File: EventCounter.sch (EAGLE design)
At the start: 23 parts, among them J1 CONN_42.54_SCREW, Q1 2N7002, Q3 DMG3404, U7 MCP6041, U8 MCP6041

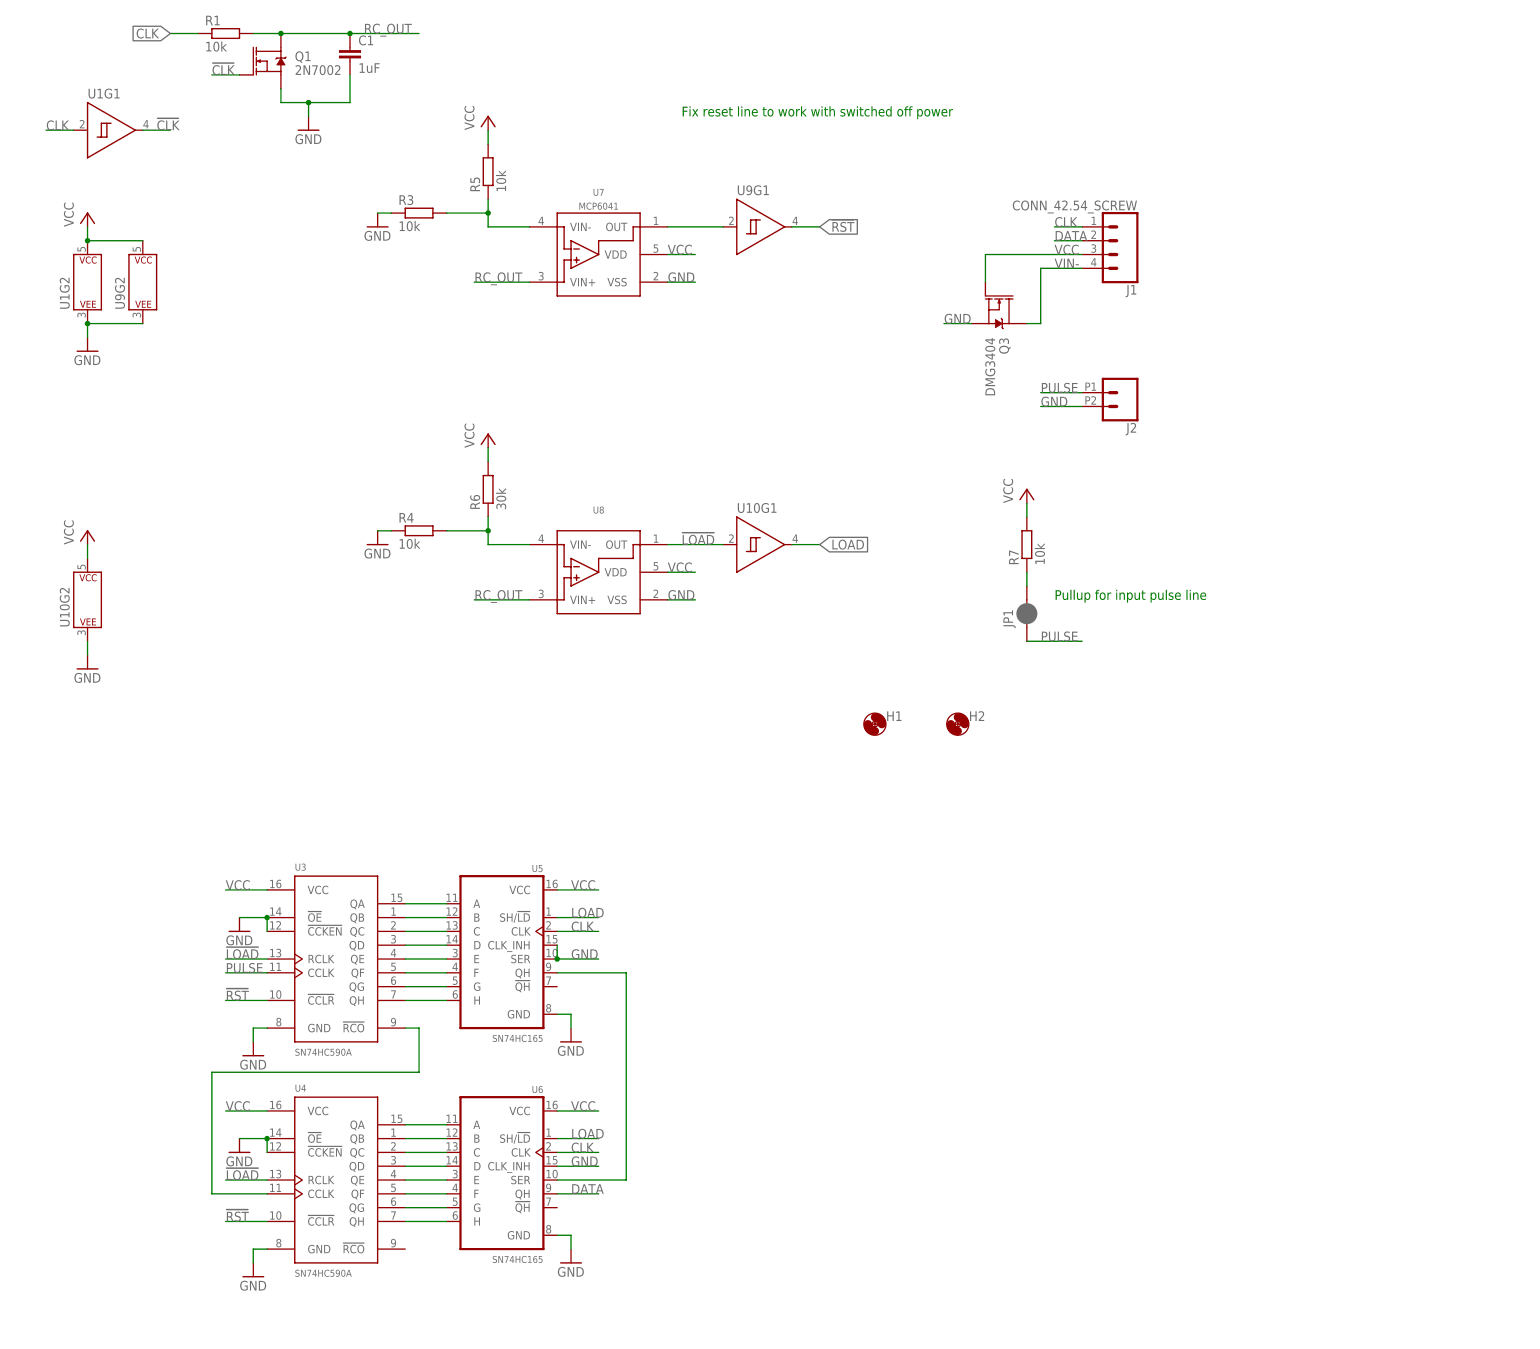
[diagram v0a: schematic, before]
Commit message: Cleaned up schematic and added frame
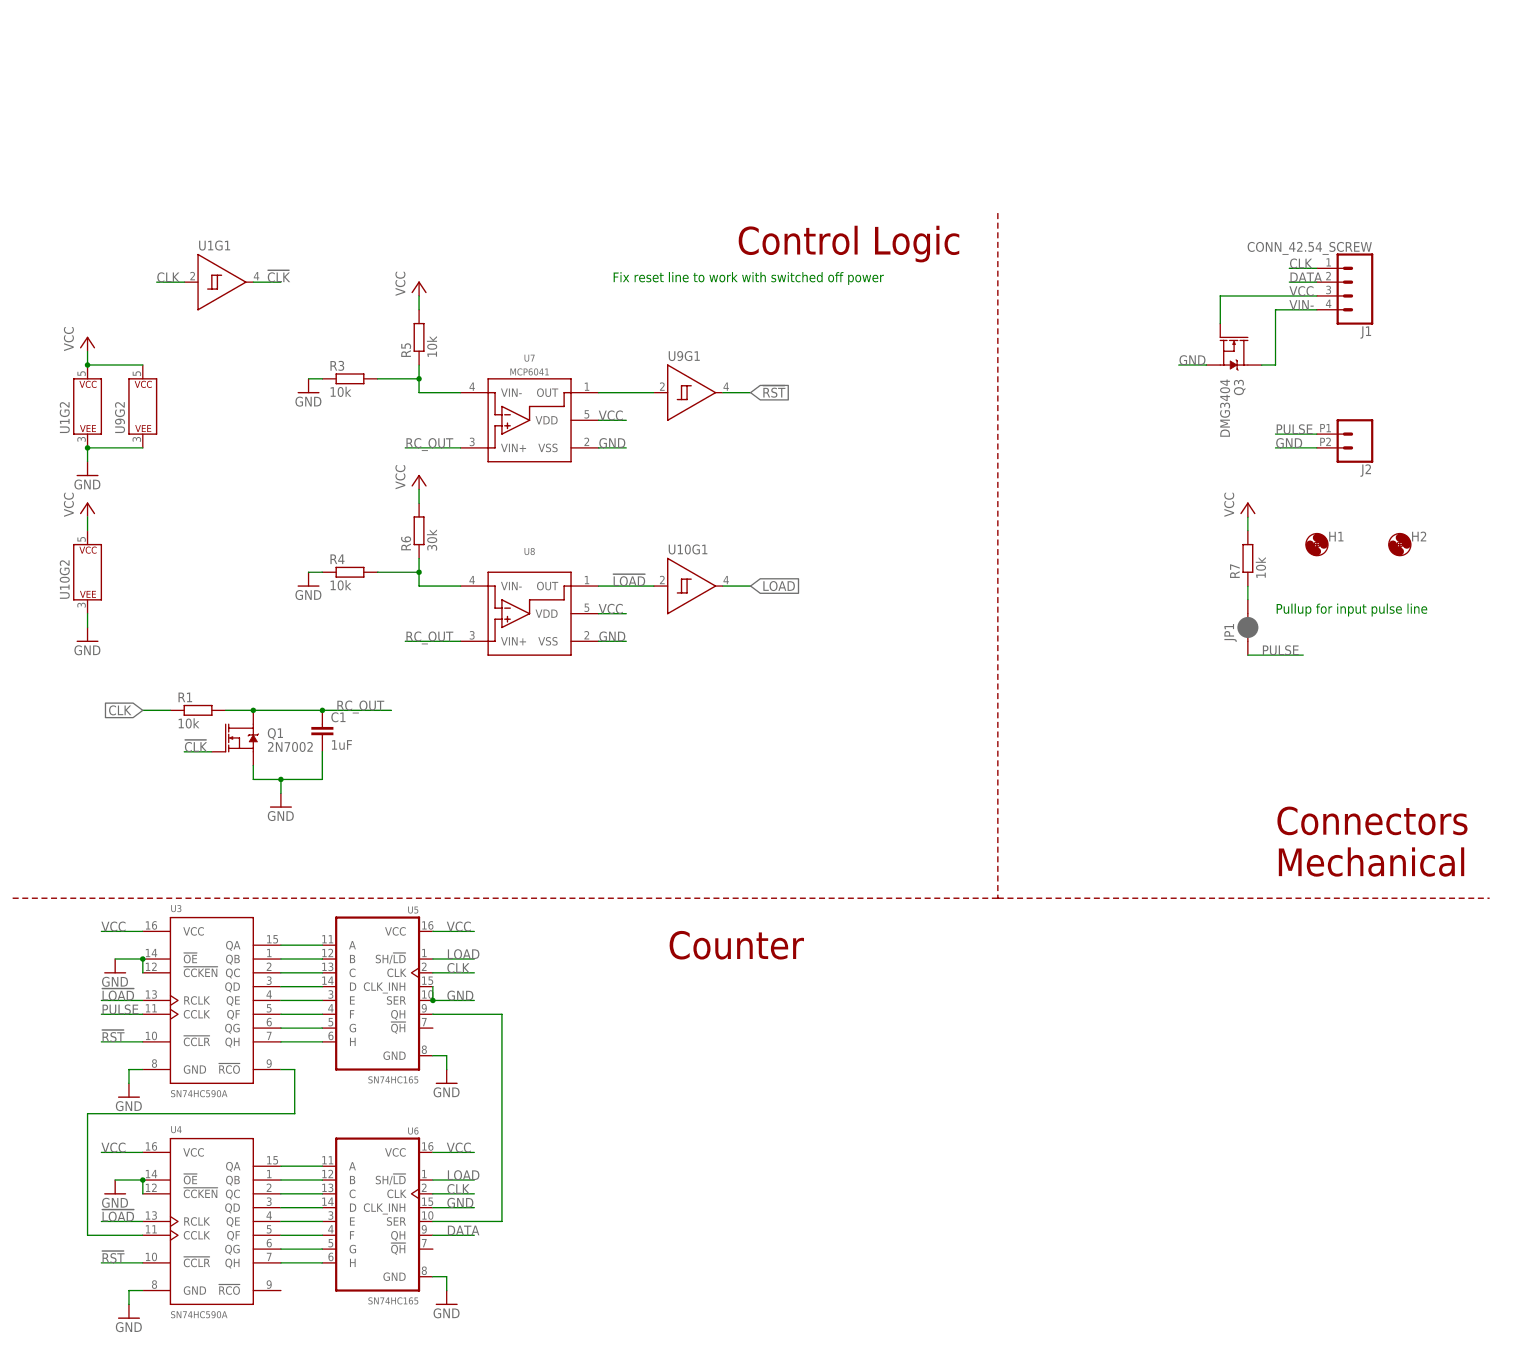
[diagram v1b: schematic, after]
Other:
- note added: "Connectors Mechanical"
- note added: "Control Logic"
- note added: "Counter"
- moved on the sheet: C1, H1, H2, J1, J2, JP1, Q1, Q3, R1, R3, R4, R5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

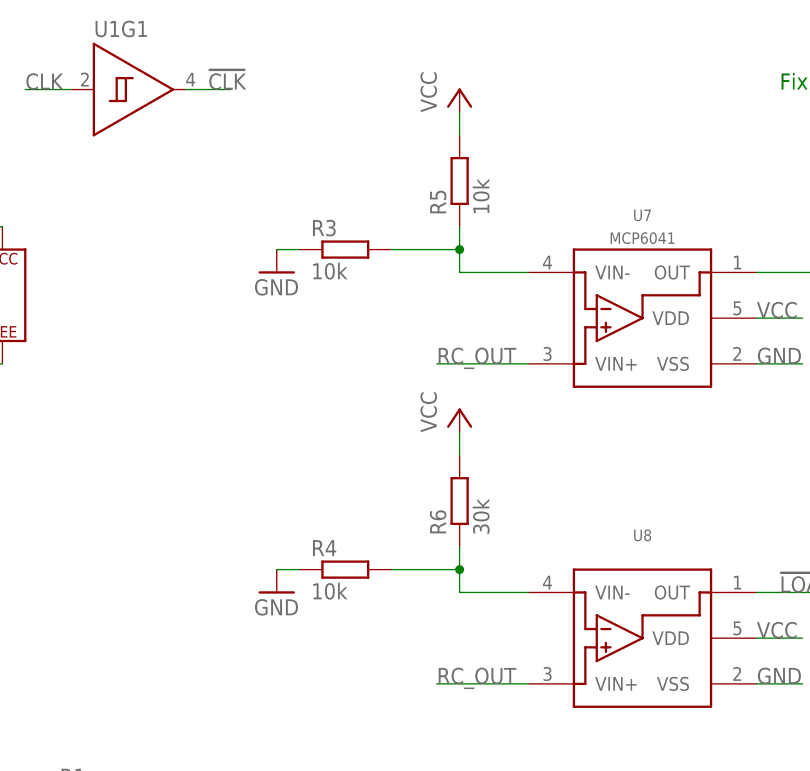
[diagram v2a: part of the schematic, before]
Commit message: Changed passive values
Changed the passive resistor divider values, need to verify with part availability
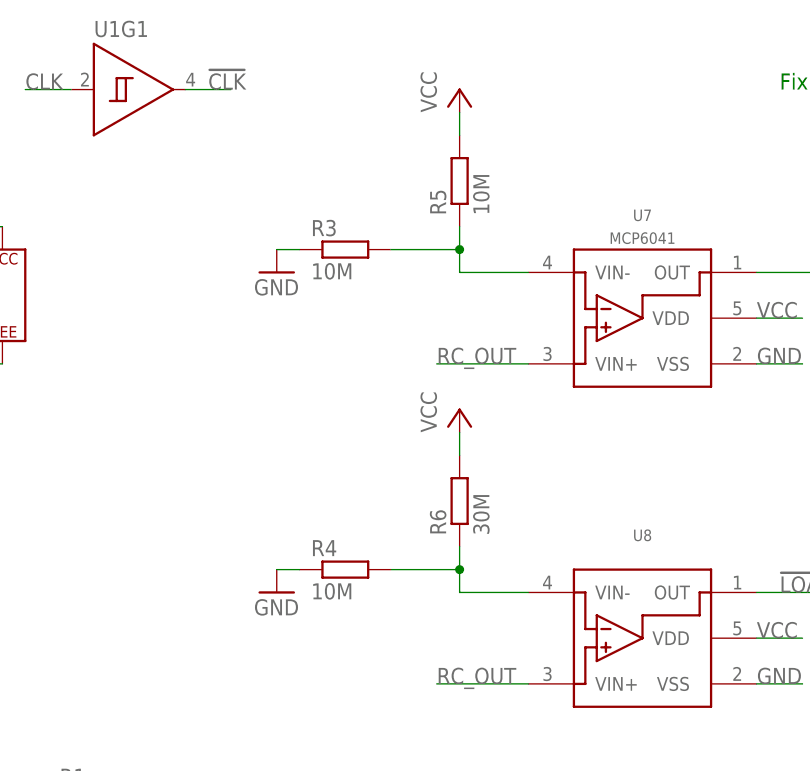
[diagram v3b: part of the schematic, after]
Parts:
- R3, R4, R5: value 10k -> 10M
- R6: value 30k -> 30M
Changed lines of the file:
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@@
 <setting verticaltext="up"/>
 </settings>
-<grid distance="0.1" unitdist="inch" unit="mm" style="lines" multiple="1" display="no" altdistance="0.01" altunitdist="inch" altunit="mm"/>
+<grid distance="0.1" unitdist="inch" unit="inch" style="lines" multiple="1" display="no" altdistance="0.01" altunitdist="inch" altunit="inch"/>
 <layers>
-<layer number="1" name="Top" color="4" fill="1" visible="yes" active="no"/>
-<layer number="2" name="Route2" color="1" fill="3" visible="yes" active="no"/>
-<layer number="3" name="Route3" color="4" fill="3" visible="yes" active="no"/>
-<layer number="4" name="Route4" color="1" fill="4" visible="yes" active="no"/>
-<layer number="5" name="Route5" color="4" fill="4" visible="yes" active="no"/>
-<layer number="6" name="Route6" color="1" fill="8" visible="yes" active="no"/>
-<layer number="7" name="Route7" color="4" fill="8" visible="yes" active="no"/>
-<layer number="8" name="Route8" color="1" fill="2" visible="yes" active="no"/>
-<layer number="9" name="Route9" color="4" fill="2" visible="yes" active="no"/>
-<layer number="10" name="Route10" color="1" fill="7" visible="yes" active="no"/>
-<layer number="11" name="Route11" color="4" fill="7" visible="yes" active="no"/>
-<layer number="12" name="Route12" color="1" fill="5" visible="yes" active="no"/>
-<layer number="13" name="Route13" color="4" fill="5" visible="yes" active="no"/>
-<layer number="14" name="Route14" color="1" fill="6" visible="yes" active="no"/>
-<layer number="15" name="Route15" color="4" fill="6" visible="yes" active="no"/>
-<layer number="16" name="Bottom" color="1" fill="1" visible="yes" active="no"/>
-<layer number="17" name="Pads" color="2" fill="1" visible="yes" active="no"/>
-<layer number="18" name="Vias" color="2" fill="1" visible="yes" active="no"/>
-<layer number="19" name="Unrouted" color="6" fill="1" visible="yes" active="no"/>
-<layer number="20" name="Dimension" color="24" fill="1" visible="yes" active="no"/>
-<layer number="21" name="tPlace" color="7" fill="1" visible="yes" active="no"/>
-<layer number="22" name="bPlace" color="7" fill="1" visible="yes" active="no"/>
-<layer number="23" name="tOrigins" color="15" fill="1" visible="yes" active="no"/>
-<layer number="24" name="bOrigins" color="15" fill="1" visible="yes" active="no"/>
-<layer number="25" name="tNames" color="7" fill="1" visible="yes" active="no"/>
-<layer number="26" name="bNames" color="7" fill="1" visible="yes" active="no"/>
-<layer number="27" name="tValues" color="7" fill="1" visible="yes" active="no"/>
-<layer number="28" name="bValues" color="7" fill="1" visible="yes" active="no"/>
+<layer number="1" name="Top" color="4" fill="1" visible="no" active="no"/>
+<layer number="2" name="Route2" color="1" fill="3" visible="no" active="no"/>
+<layer number="3" name="Route3" color="4" fill="3" visible="no" active="no"/>
+<layer number="4" name="Route4" color="1" fill="4" visible="no" active="no"/>
+<layer number="5" name="Route5" color="4" fill="4" visible="no" active="no"/>
+<layer number="6" name="Route6" color="1" fill="8" visible="no" active="no"/>
+<layer number="7" name="Route7" color="4" fill="8" visible="no" active="no"/>
+<layer number="8" name="Route8" color="1" fill="2" visible="no" active="no"/>
+<layer number="9" name="Route9" color="4" fill="2" visible="no" active="no"/>
+<layer number="10" name="Route10" color="1" fill="7" visible="no" active="no"/>
+<layer number="11" name="Route11" color="4" fill="7" visible="no" active="no"/>
+<layer number="12" name="Route12" color="1" fill="5" visible="no" active="no"/>
+<layer number="13" name="Route13" color="4" fill="5" visible="no" active="no"/>
+<layer number="14" name="Route14" color="1" fill="6" visible="no" active="no"/>
+<layer number="15" name="Route15" color="4" fill="6" visible="no" active="no"/>
+<layer number="16" name="Bottom" color="1" fill="1" visible="no" active="no"/>
+<layer number="17" name="Pads" color="2" fill="1" visible="no" active="no"/>
+<layer number="18" name="Vias" color="2" fill="1" visible="no" active="no"/>
+<layer number="19" name="Unrouted" color="6" fill="1" visible="no" active="no"/>
+<layer number="20" name="Dimension" color="24" fill="1" visible="no" active="no"/>
+<layer number="21" name="tPlace" color="7" fill="1" visible="no" active="no"/>
+<layer number="22" name="bPlace" color="7" fill="1" visible="no" active="no"/>
+<layer number="23" name="tOrigins" color="15" fill="1" visible="no" active="no"/>
+<layer number="24" name="bOrigins" color="15" fill="1" visible="no" active="no"/>
+<layer number="25" name="tNames" color="7" fill="1" visible="no" active="no"/>
+<layer number="26" name="bNames" color="7" fill="1" visible="no" active="no"/>
+<layer number="27" name="tValues" color="7" fill="1" visible="no" active="no"/>
+<layer number="28" name="bValues" color="7" fill="1" visible="no" active="no"/>
 <layer number="29" name="tStop" color="7" fill="3" visible="no" active="no"/>
 <layer number="30" name="bStop" color="7" fill="6" visible="no" active="no"/>
@@
 <layer number="35" name="tGlue" color="7" fill="4" visible="no" active="no"/>
 <layer number="36" name="bGlue" color="7" fill="5" visible="no" active="no"/>
-<layer number="37" name="tTest" color="7" fill="1" visible="yes" active="no"/>
-<layer number="38" name="bTest" color="7" fill="1" visible="yes" active="no"/>
+<layer number="37" name="tTest" color="7" fill="1" visible="no" active="no"/>
+<layer number="38" name="bTest" color="7" fill="1" visible="no" active="no"/>
 <layer number="39" name="tKeepout" color="4" fill="11" visible="no" active="no"/>
 <layer number="40" name="bKeepout" color="1" fill="11" visible="no" active="no"/>
@@
 <layer number="44" name="Drills" color="7" fill="1" visible="no" active="no"/>
 <layer number="45" name="Holes" color="7" fill="1" visible="no" active="no"/>
-<layer number="46" name="Milling" color="3" fill="1" visible="yes" active="no"/>
-<layer number="47" name="Measures" color="7" fill="1" visible="yes" active="no"/>
-<layer number="48" name="Document" color="7" fill="1" visible="yes" active="no"/>
-<layer number="49" name="Reference" color="7" fill="1" visible="yes" active="no"/>
-<layer number="50" name="dxf" color="7" fill="1" visible="yes" active="no"/>
-<layer number="51" name="tDocu" color="7" fill="1" visible="yes" active="no"/>
-<layer number="52" name="bDocu" color="7" fill="1" visible="yes" active="no"/>
-<layer number="53" name="tGND_GNDA" color="7" fill="1" visible="yes" active="no"/>
-<layer number="54" name="bGND_GNDA" color="7" fill="1" visible="yes" active="no"/>
-<layer number="56" name="wert" color="7" fill="1" visible="yes" active="no"/>
-<layer number="57" name="tCAD" color="7" fill="1" visible="yes" active="no"/>
-<layer number="59" name="tCarbon" color="7" fill="1" visible="yes" active="no"/>
-<layer number="60" name="bCarbon" color="7" fill="1" visible="yes" active="no"/>
+<layer number="46" name="Milling" color="3" fill="1" visible="no" active="no"/>
+<layer number="47" name="Measures" color="7" fill="1" visible="no" active="no"/>
+<layer number="48" name="Document" color="7" fill="1" visible="no" active="no"/>
+<layer number="49" name="Reference" color="7" fill="1" visible="no" active="no"/>
+<layer number="50" name="dxf" color="7" fill="1" visible="no" active="no"/>
+<layer number="51" name="tDocu" color="7" fill="1" visible="no" active="no"/>
+<layer number="52" name="bDocu" color="7" fill="1" visible="no" active="no"/>
+<layer number="53" name="tGND_GNDA" color="7" fill="1" visible="no" active="no"/>
+<layer number="54" name="bGND_GNDA" color="7" fill="1" visible="no" active="no"/>
+<layer number="56" name="wert" color="7" fill="1" visible="no" active="no"/>
+<layer number="57" name="tCAD" color="7" fill="1" visible="no" active="no"/>
+<layer number="59" name="tCarbon" color="7" fill="1" visible="no" active="no"/>
+<layer number="60" name="bCarbon" color="7" fill="1" visible="no" active="no"/>
 <layer number="88" name="SimResults" color="9" fill="1" visible="yes" active="yes"/>
 <layer number="89" name="SimProbes" color="9" fill="1" visible="yes" active="yes"/>
@@
 <attribute name="DISP" value="MCP6041"/>
 </part>
-<part name="R4" library="bschulz_passives" deviceset="R-EU_" device="R0603" technology="10K" value="10k"/>
-<part name="R6" library="bschulz_passives" deviceset="R-EU_" device="R0603" value="30k"/>
+<part name="R4" library="bschulz_passives" deviceset="R-EU_" device="R0603" technology="10K" value="10M"/>
+<part name="R6" library="bschulz_passives" deviceset="R-EU_" device="R0603" value="30M"/>
 <part name="GND8" library="supply1" library_urn="urn:adsk.eagle:library:371" deviceset="GND" device=""/>
 <part name="P+4" library="supply1" library_urn="urn:adsk.eagle:library:371" deviceset="VCC" device=""/>
@@
 <part name="U1" library="bschulz" deviceset="SN74*1G14" device="DCK" technology="LVC"/>
 <part name="R1" library="bschulz_passives" deviceset="R-EU_" device="R0603" technology="10K" value="10k"/>
-<part name="R3" library="bschulz_passives" deviceset="R-EU_" device="R0603" technology="10K" value="10k"/>
-<part name="R5" library="bschulz_passives" deviceset="R-EU_" device="R0603" value="10k"/>
+<part name="R3" library="bschulz_passives" deviceset="R-EU_" device="R0603" technology="10K" value="10M"/>
+<part name="R5" library="bschulz_passives" deviceset="R-EU_" device="R0603" value="10M"/>
 <part name="GND7" library="supply1" library_urn="urn:adsk.eagle:library:371" deviceset="GND" device=""/>
 <part name="P+3" library="supply1" library_urn="urn:adsk.eagle:library:371" deviceset="VCC" device=""/>
